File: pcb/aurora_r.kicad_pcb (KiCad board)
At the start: 2 copper layers, 154 x 114.2 mm, 122 parts

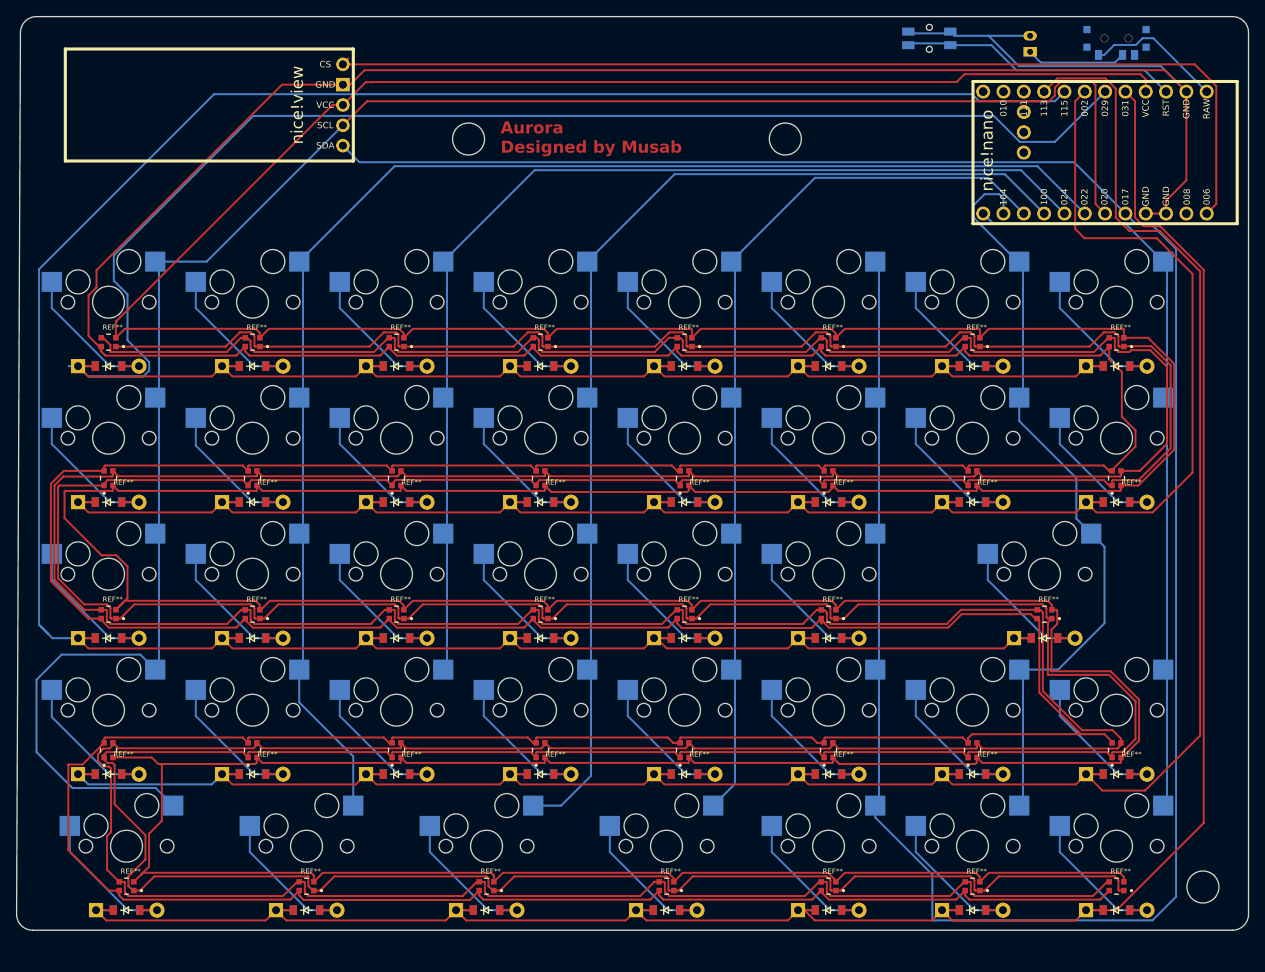
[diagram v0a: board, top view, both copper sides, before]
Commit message: Add stab holes and extended base to PCB
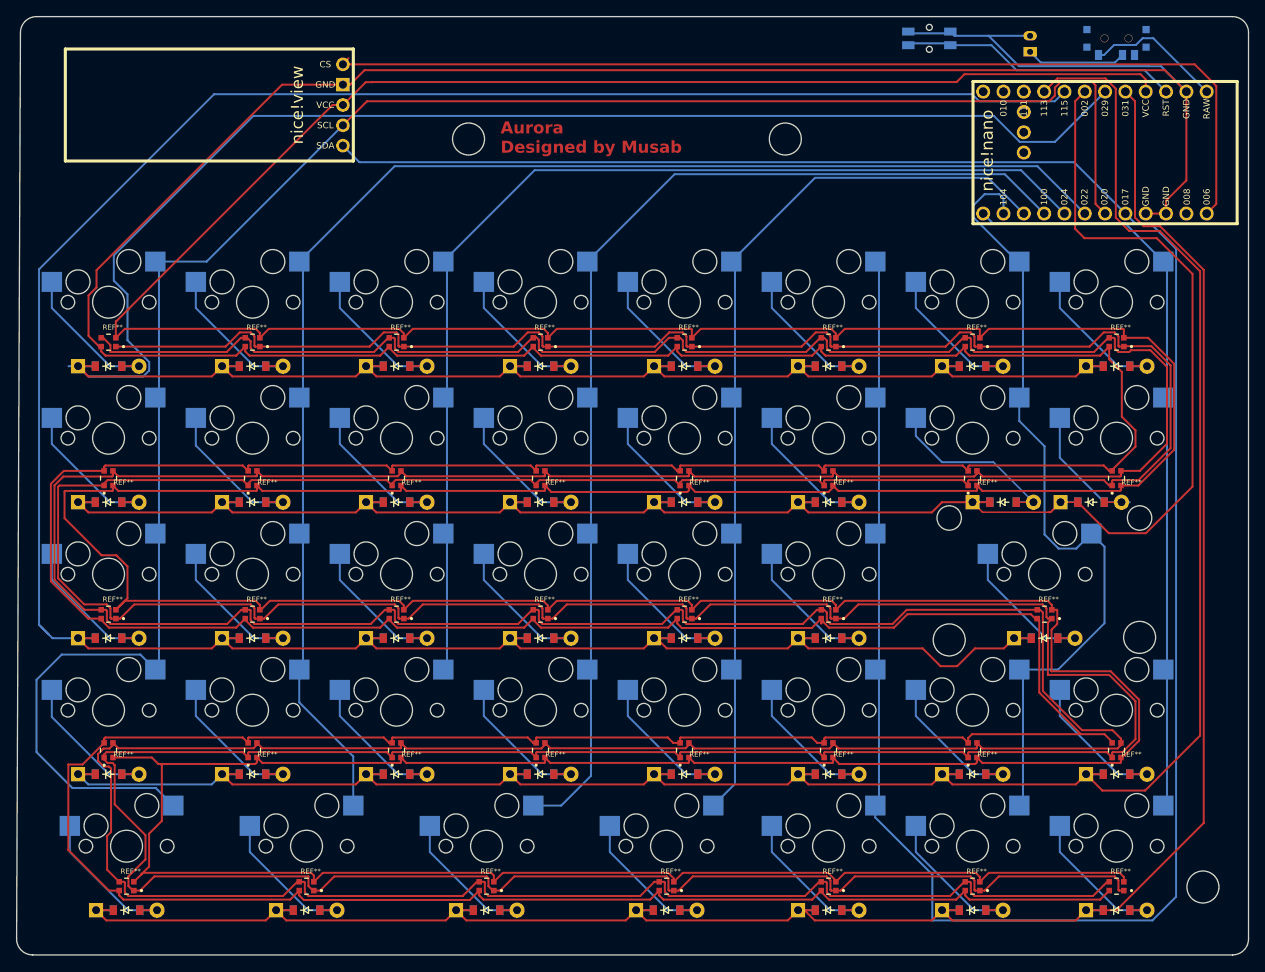
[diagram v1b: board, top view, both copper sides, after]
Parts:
- added REF**: SW_Cherry_MX_2.00u_PCB, Button_Switch_Keyboard:SW_Cherry_MX_2.00u_PCB, F.Cu at (219.5, 111.9)
- moved D13 3.81 mm to (211.8, 108.0)
- moved D15 3.19 mm to (222.8, 108.0)
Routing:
- net seven_top: track 19.3 -> 24.7 mm
- net P104: track 96.4 -> 101.4 mm
- net P002: track 243.4 -> 246.4 mm
- net P115: track 343.1 -> 345.0 mm
- net eight_top: track 19.3 -> 18.6 mm
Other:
- board size 154 x 114.2 mm -> 154 x 117.3 mm
